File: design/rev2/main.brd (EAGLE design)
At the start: 78 x 50 mm, 44 parts, among them J1 ICSP-HEADER1X6-0.1-ICSP-PADS, J2 HEADER-141X14-0.05-PADS, SW1 B3U-3000P, U1 PIC18F2XK20, U2 LIS3DSH, U3 APDS-9008, U4 APDS-9008

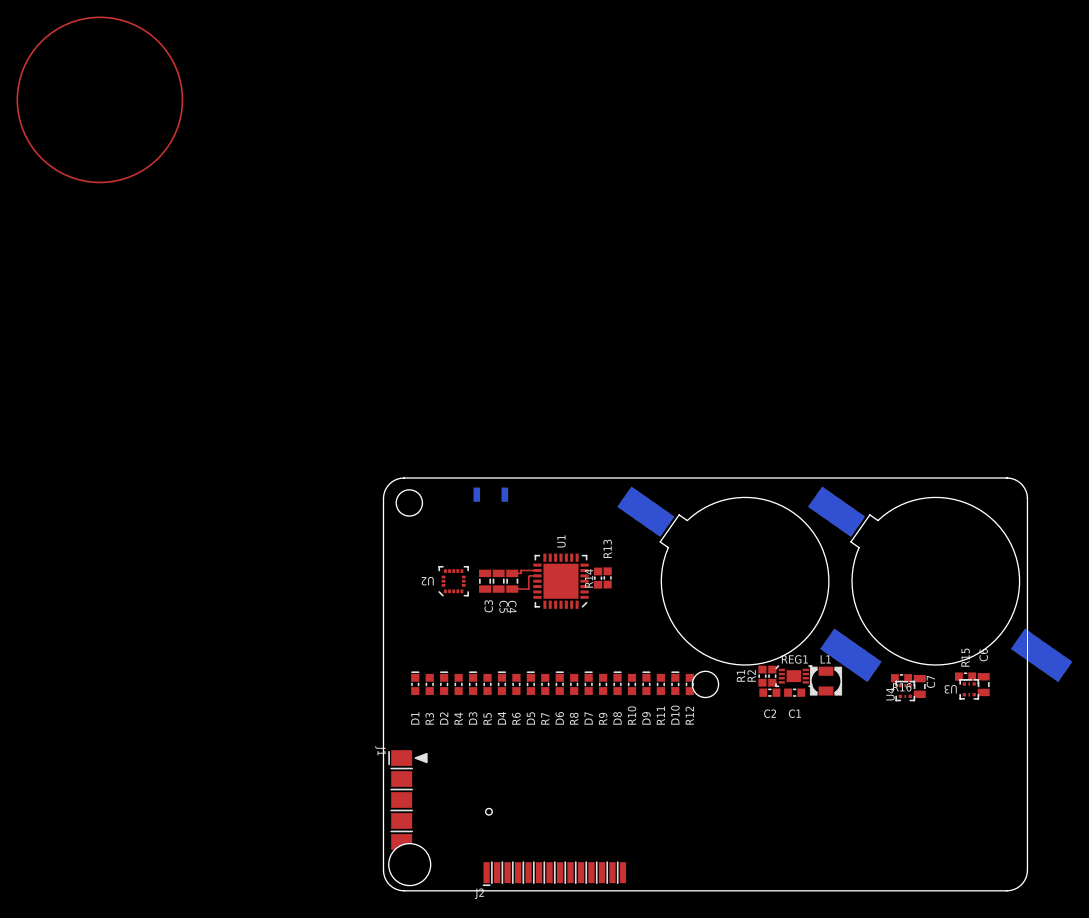
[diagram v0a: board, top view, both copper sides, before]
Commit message: [CNG] - finished most routing on rev2, added new mechanical drawings (not up to date with POR)
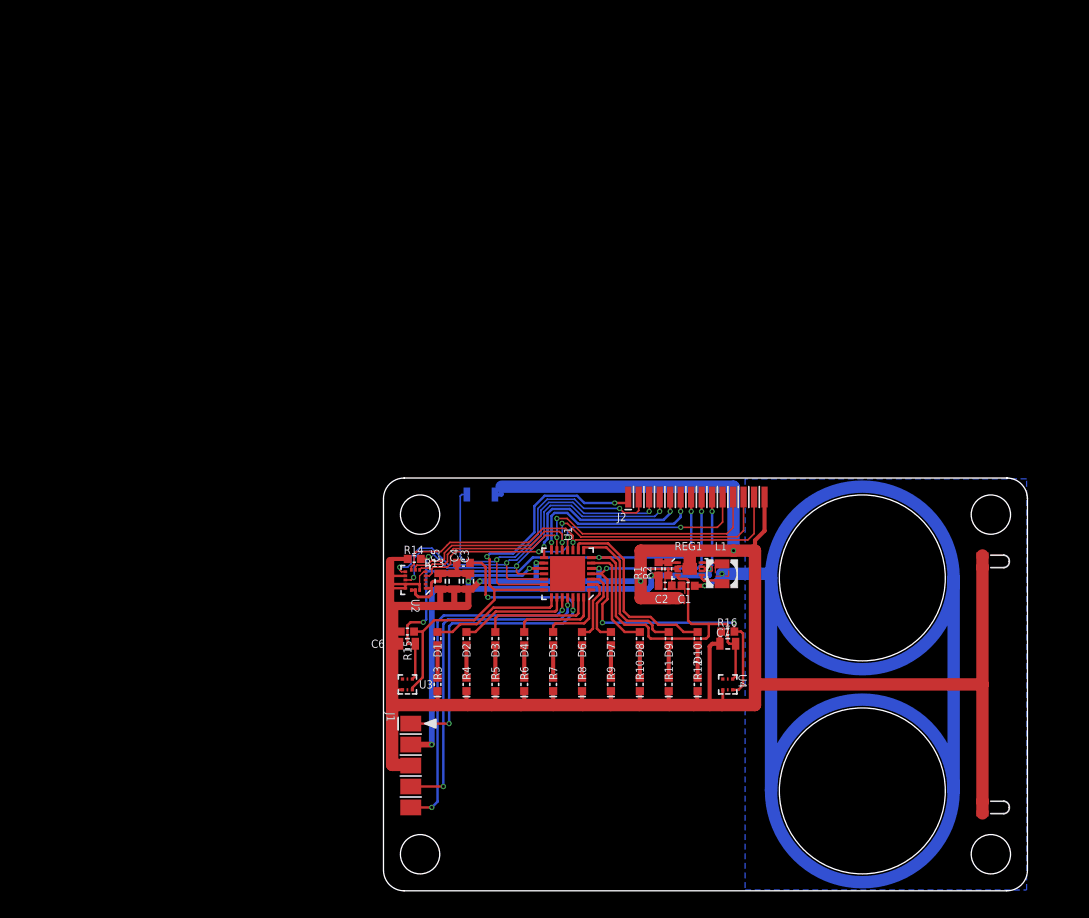
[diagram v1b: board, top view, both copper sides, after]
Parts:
- added X1, X2: TE-2199248-X, matt:TE-2199248-X
- B1, B2: value BATTERYCR-2016/F2N -> BATTERY-POS-HALF; device matt:CR-2016/F2N -> matt:CR20XX-PLATED
- moved C6 70.0 mm to (2.90, 29.9), turned to 0 degrees
- moved U3 68.1 mm to (2.90, 25.0), turned to 0 degrees
- moved R15 67.8 mm to (2.90, 31.4), turned to 0 degrees
- moved J2 48.6 mm to (37.9, 47.7)
- moved B1 26.9 mm to (58.0, 12.1), turned to 90 degrees
- moved C7 23.8 mm to (41.7, 29.9), turned to 0 degrees
- moved R14 22.4 mm to (3.73, 40.2), turned to 0 degrees
- moved R16 21.8 mm to (41.7, 31.4), turned to 0 degrees
- moved U4 21.5 mm to (41.7, 25.0), turned to 0 degrees
- moved C1 18.3 mm to (36.9, 37.0)
- moved C2 18.1 mm to (34.1, 37.0)
- moved L1 18.1 mm to (41.0, 38.4)
- moved R2 18.1 mm to (34.5, 39.0)
- moved REG1 18.1 mm to (37.1, 39.0)
- moved R1 18.1 mm to (33.3, 39.0)
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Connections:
- net +3V3: now also J2.P$9; no longer J2.P$8
- net ACCEL_INT2: now also J2.P$3; no longer J2.P$5
- net ALS_VSENSE_CLK: now also J2.P$1; no longer J2.P$7
- net ALS_VSENSE_DAT: now also J2.P$8; no longer J2.P$6
- net BOOST_EN: now also J2.P$7; no longer J2.P$14
- net GND: now also J2.P$14, X1.P$1, X1.P$2, X2.P$1, X2.P$2; no longer B1.P$-, B2.P$-, J2.P$1
- net PIC_EXT_FUNC: now also J2.P$2; no longer J2.P$9
- net PIC_RX: now also J2.P$5; no longer J2.P$3
- net PIC_TX: now also J2.P$6; no longer J2.P$2
- net V_BATT: now also B1.P$1, B2.P$1; no longer B1.P$+, B2.P$+
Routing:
- net GND: track 3.37 -> 318.1 mm, vias 0 -> 5
- net BOOST_EN: track 0.00 -> 102.0 mm, vias 0 -> 4
- net +3V3: track 4.59 -> 92.2 mm, vias 0 -> 6
- net V_BATT: track 0.00 -> 64.2 mm, vias 0 -> 2
- net ALS_VSENSE_DAT: track 0.00 -> 54.4 mm, vias 0 -> 4
- net ALS_VSENSE_CLK: track 0.00 -> 53.7 mm, vias 0 -> 2
- net PIC_SDI: track 0.00 -> 51.8 mm, vias 0 -> 2
- net PIC_CS: track 0.00 -> 51.6 mm, vias 0 -> 1
- net ICSP_!MCLR!: track 0.00 -> 51.4 mm, vias 0 -> 3
- net PIC_SDO: track 0.00 -> 48.9 mm, vias 0 -> 2
- net ACCEL_INT2: track 0.00 -> 47.3 mm, vias 0 -> 3
- net ACCEL_INT1: track 0.00 -> 46.1 mm, vias 0 -> 3
- net PIC_EXT_FUNC: track 0.00 -> 46.1 mm, vias 0 -> 2
- net PIC_SCK: track 0.00 -> 45.2 mm, vias 0 -> 3
- net ICSP_CLK: track 0.00 -> 42.6 mm, vias 0 -> 2
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- added copper zone on layer 1, net +3V3
- added copper zone on layer 1, net GND
- added copper zone on layer 1, net V_BATT
- added copper zone on layer 16, net V_BATT
